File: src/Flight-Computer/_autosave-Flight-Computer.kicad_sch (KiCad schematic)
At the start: 32 parts, among them J1 Jumper_NO, P8 3220-20-0200-00, U1 STM32H750VBTx, Y1 ECS-240-18-33-JGN-TR

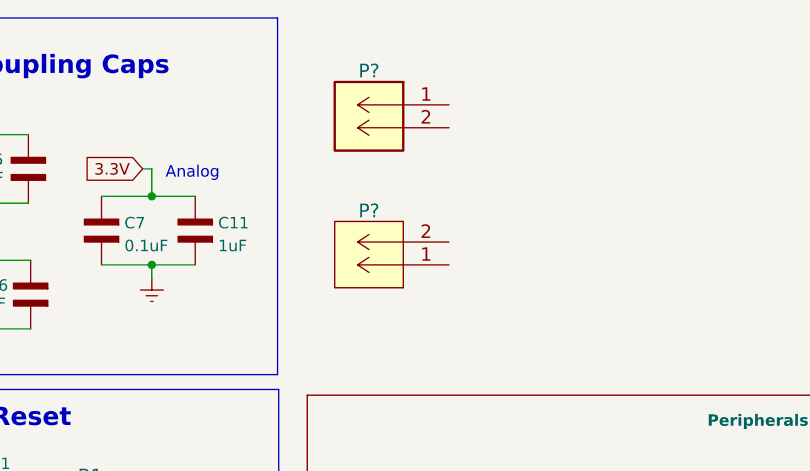
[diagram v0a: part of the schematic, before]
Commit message: added schottky diode to lib files
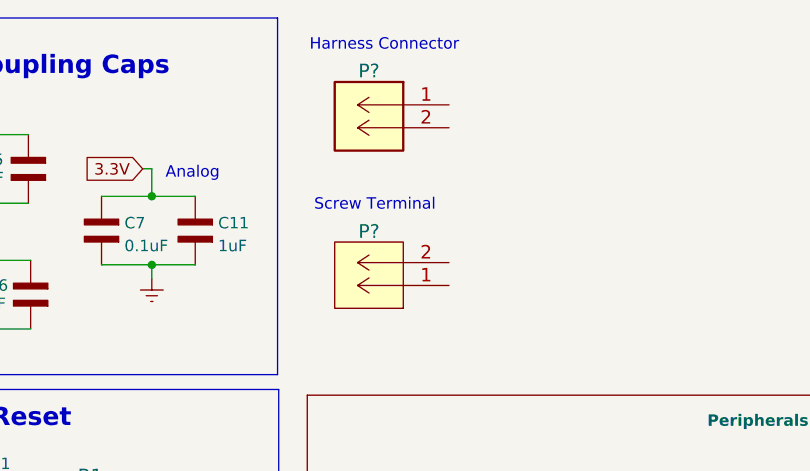
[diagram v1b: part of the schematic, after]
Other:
- note added: "Harness Connector"
- note added: "Screw Terminal"
- moved on the sheet: P?
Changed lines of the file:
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@@
+    (effects (font (size 1.27 1.27)) (justify left bottom))
+  )
+  (text "Screw Terminal" (at 178.054 40.64 0)
     (effects (font (size 1.27 1.27)) (justify left bottom))
   )
   (text "Microcontroller" (at 52.07 27.94 0)
     (effects (font (size 2.032 2.032) (thickness 0.4064) bold) (justify left bottom))
+  )
+  (text "Harness Connector" (at 177.546 22.86 0)
+    (effects (font (size 1.27 1.27)) (justify left bottom))
   )
   (text "Digital" (at 132.588 30.48 0)
@@
     (pin "2")
   )
-  (symbol (lib_id "Flight-Computer:282837-2") (at 193.04 46.482 180) (unit 1)
-    (in_bom yes) (on_board yes) (fields_autoplaced)
-    (property "Reference" "P?" (id 0) (at 184.15 40.4891 0)
+  (symbol (lib_id "Flight-Computer:282837-2") (at 193.04 48.768 180) (unit 1)
+    (in_bom yes) (on_board yes) (fields_autoplaced)
+    (property "Reference" "P?" (id 0) (at 184.15 42.7751 0)
       (effects (font (size 1.524 1.524)))
     )
-    (property "Value" "282837-2" (id 1) (at 187.96 18.542 0)
+    (property "Value" "282837-2" (id 1) (at 187.96 20.828 0)
       (effects (font (size 1.524 1.524)) hide)
     )
-    (property "Footprint" "66953-005LF_AMP" (id 2) (at 189.23 16.002 0)
+    (property "Footprint" "66953-005LF_AMP" (id 2) (at 189.23 18.288 0)
       (effects (font (size 1.524 1.524)) hide)
     )
-    (property "Datasheet" "" (id 3) (at 193.04 46.482 0)
+    (property "Datasheet" "" (id 3) (at 193.04 48.768 0)
       (effects (font (size 1.524 1.524)) hide)
     )
